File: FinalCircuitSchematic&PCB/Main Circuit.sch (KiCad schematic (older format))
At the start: 86 parts, among them IC1 LTC3895IFE#TRPBF, J1 Conn_01x02_Male, J2 Conn_01x02_Male, J3 Conn_01x02_Male, J4 Raspberry_Pi_2_3, J5 Conn_01x02_Male, J6 Conn_01x02_Male, J7 Conn_01x02_Male, J8 Conn_01x02_Male, Q1 PN2222A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

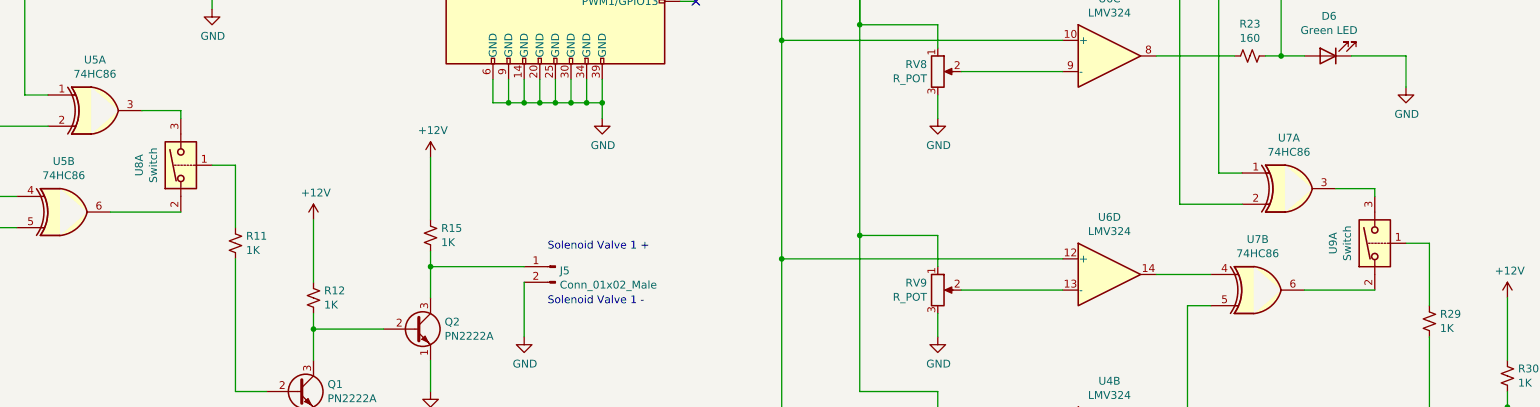
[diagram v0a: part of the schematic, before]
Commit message: Updated final schematic as incorrect switch packages were selected. Added external switch library
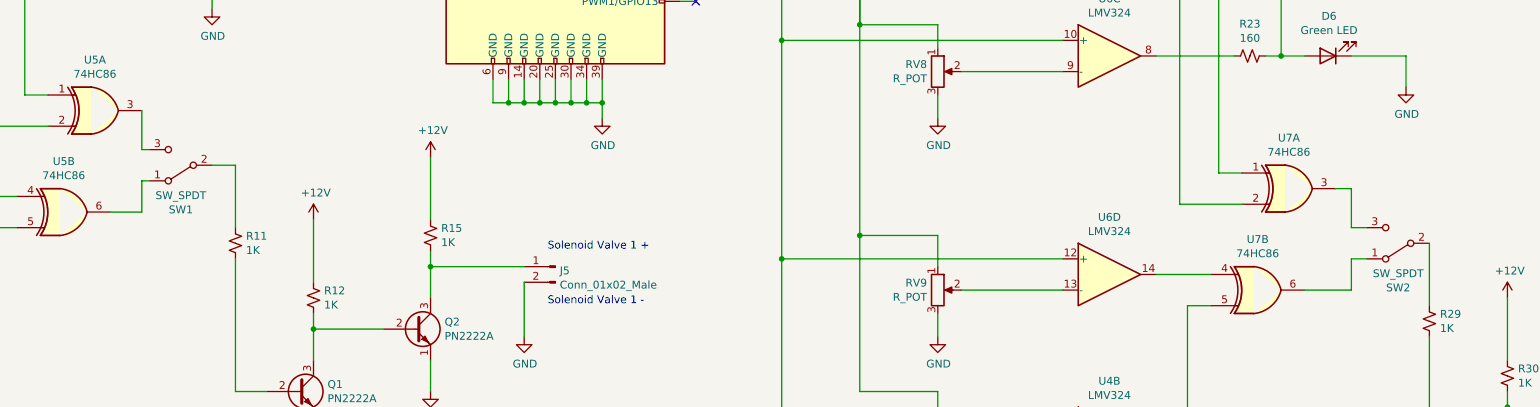
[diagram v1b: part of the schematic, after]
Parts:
- removed U8, U9: Switch, Package_SO:QSOP-16_3.9x4.9mm_P0.635mm, symbol Analog_Switch:DG308AxY
- added SW1, SW2: SW_SPDT, Button_Switch_SMD:JS102011JCQN, symbol Switch:SW_SPDT
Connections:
- net at R29.1: now also SW2.2 (B)
- net at U7.6: now also SW2.1 (A)
- net at U7.3: now also SW2.3 (C)
- net at R11.1: now also SW1.2 (B)
- net at U5.3: now also SW1.3 (C)
- net at U5.6: now also SW1.1 (A)
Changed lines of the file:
@@
 EESchema Schematic File Version 4
-LIBS:Main Circuit-cache
-EELAYER 29 0
+EELAYER 30 0
 EELAYER END
 $Descr A2 23386 16535
@@
 Wire Wire Line
 	4900 11600 5250 11600
-Wire Wire Line
-	5850 11700 6300 11700
-Wire Wire Line
-	6050 11050 6300 11050
-Wire Wire Line
-	6300 11050 6300 11100
 $Comp
 L 74xx:74HC86 U5
@@
 Wire Wire Line
 	12550 12100 12900 12100
-Wire Wire Line
-	13500 12200 13950 12200
-Wire Wire Line
-	13700 11550 13950 11550
-Wire Wire Line
-	13950 11550 13950 11600
 $Comp
 L 74xx:74HC86 U7
@@
 $EndComp
 Wire Wire Line
-	14150 11900 14300 11900
-Wire Wire Line
 	14300 11900 14300 12300
 Wire Wire Line
@@
 	1    0    0    -1
 $EndComp
-$Comp
-L Analog_Switch:DG308AxY U8
-U 1 1 60C9EA52
-P 6300 11400
-F 0 "U8" H 6300 11667 50  0000 C CNN
-F 1 "Switch" H 6300 11576 50  0000 C CNN
-F 2 "Package_SO:QSOP-16_3.9x4.9mm_P0.635mm" H 6300 11300 50  0001 C CNN
-F 3 "http://pdf.datasheetcatalog.com/datasheets/70/494502_DS.pdf" H 6300 11400 50  0001 C CNN
-	1    6300 11400
-	0    -1   -1   0
-$EndComp
 Wire Wire Line
 	3000 9500 3000 10000
@@
 $EndComp
 $Comp
-L Analog_Switch:DG308AxY U9
-U 1 1 60BAE308
-P 13950 11900
-F 0 "U9" H 13950 12167 50  0000 C CNN
-F 1 "Switch" H 13950 12076 50  0000 C CNN
-F 2 "Package_SO:QSOP-16_3.9x4.9mm_P0.635mm" H 13950 11800 50  0001 C CNN
-F 3 "http://pdf.datasheetcatalog.com/datasheets/70/494502_DS.pdf" H 13950 11900 50  0001 C CNN
-	1    13950 11900
-	0    -1   -1   0
-$EndComp
-$Comp
 L power:+5V #PWR0101
 U 1 1 60CEC062
@@
 	-1   0    0    -1
 $EndComp
+$Comp
+L Switch:SW_SPDT SW2
+U 1 1 60CA8509
+P 14100 11900
+F 0 "SW2" H 14100 12185 50  0000 C CNN
+F 1 "SW_SPDT" H 14100 12094 50  0000 C CNN
+F 2 "Button_Switch_SMD:JS102011JCQN" H 14100 11900 50  0001 C CNN
+F 3 "~" H 14100 11900 50  0001 C CNN
+	1    14100 11900
+	-1   0    0    1
+$EndComp
+Wire Wire Line
+	13500 12200 13800 12200
+Wire Wire Line
+	13800 12200 13800 12000
+Wire Wire Line
+	13800 12000 13900 12000
+Wire Wire Line
+	13900 11800 13800 11800
+Wire Wire Line
+	13800 11800 13800 11550
+Wire Wire Line
+	13800 11550 13700 11550
+$Comp
+L Switch:SW_SPDT SW1
+U 1 1 60DD0185
+P 6300 11400
+F 0 "SW1" H 6300 11685 50  0000 C CNN
+F 1 "SW_SPDT" H 6300 11594 50  0000 C CNN
+F 2 "Button_Switch_SMD:JS102011JCQN" H 6300 11400 50  0001 C CNN
+F 3 "~" H 6300 11400 50  0001 C CNN
+	1    6300 11400
+	-1   0    0    1
+$EndComp
+Wire Wire Line
+	6050 11050 6050 11300
+Wire Wire Line
+	6050 11300 6100 11300
+Wire Wire Line
+	5850 11700 6050 11700
+Wire Wire Line
+	6050 11700 6050 11500
+Wire Wire Line
+	6050 11500 6100 11500
 $EndSCHEMATC
